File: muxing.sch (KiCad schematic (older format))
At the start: 0 parts

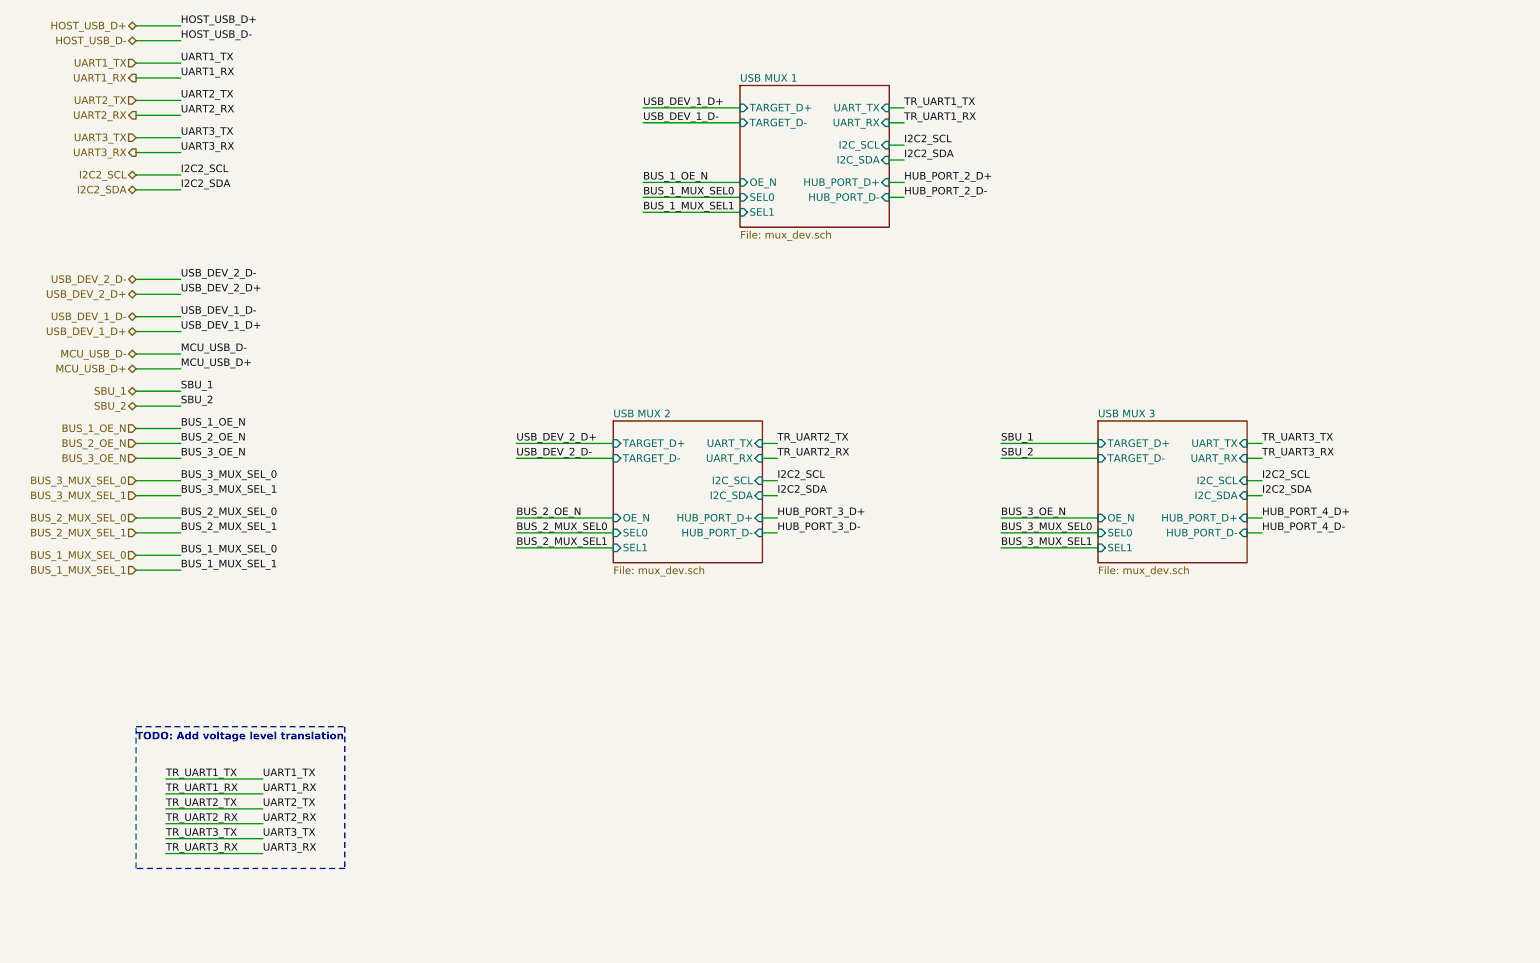
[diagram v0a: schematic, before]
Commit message: Complete muxing and level translation
Added Aux USB to avoid using a HUB, which don't seem to be too readily
available out there and would complicate the design for no good reason.

Now the i2c lines can also be switched.

Added voltage level translation up to 1.2V from 3.3V. Selected
bidirectional level translator.

Started looking into power supply.
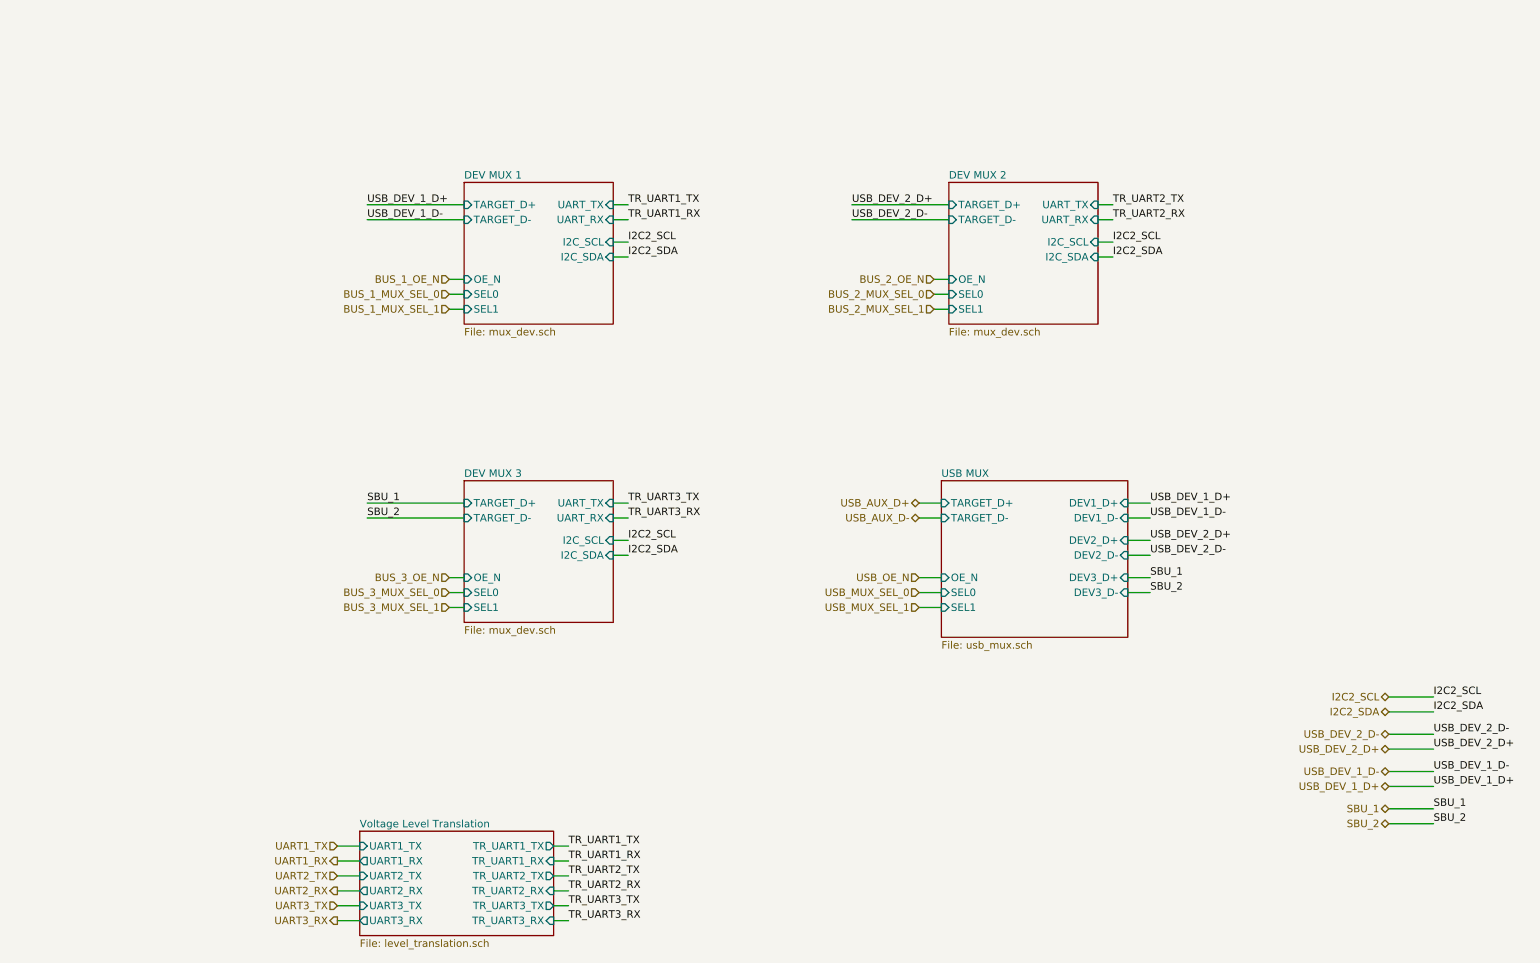
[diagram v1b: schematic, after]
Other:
- note removed: "TODO: Add voltage level translation"

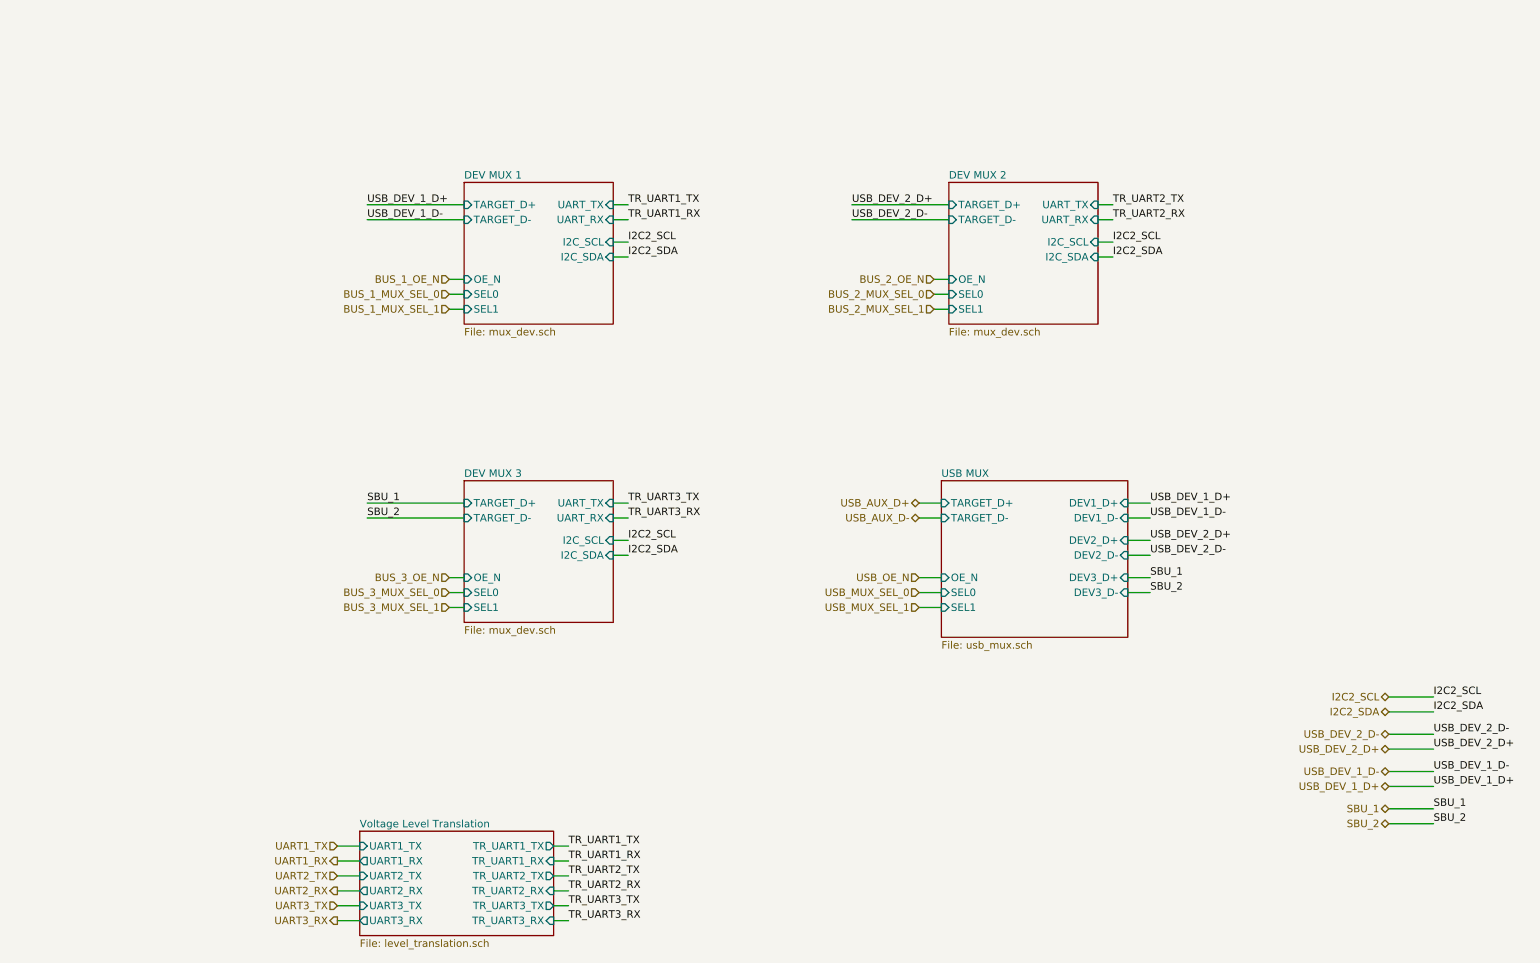
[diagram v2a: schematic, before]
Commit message: Supply caps, initial signal states and headers
  * Added bulk supply caps.
  * Set initial control signal states via resistors.
  * Add debug headers.
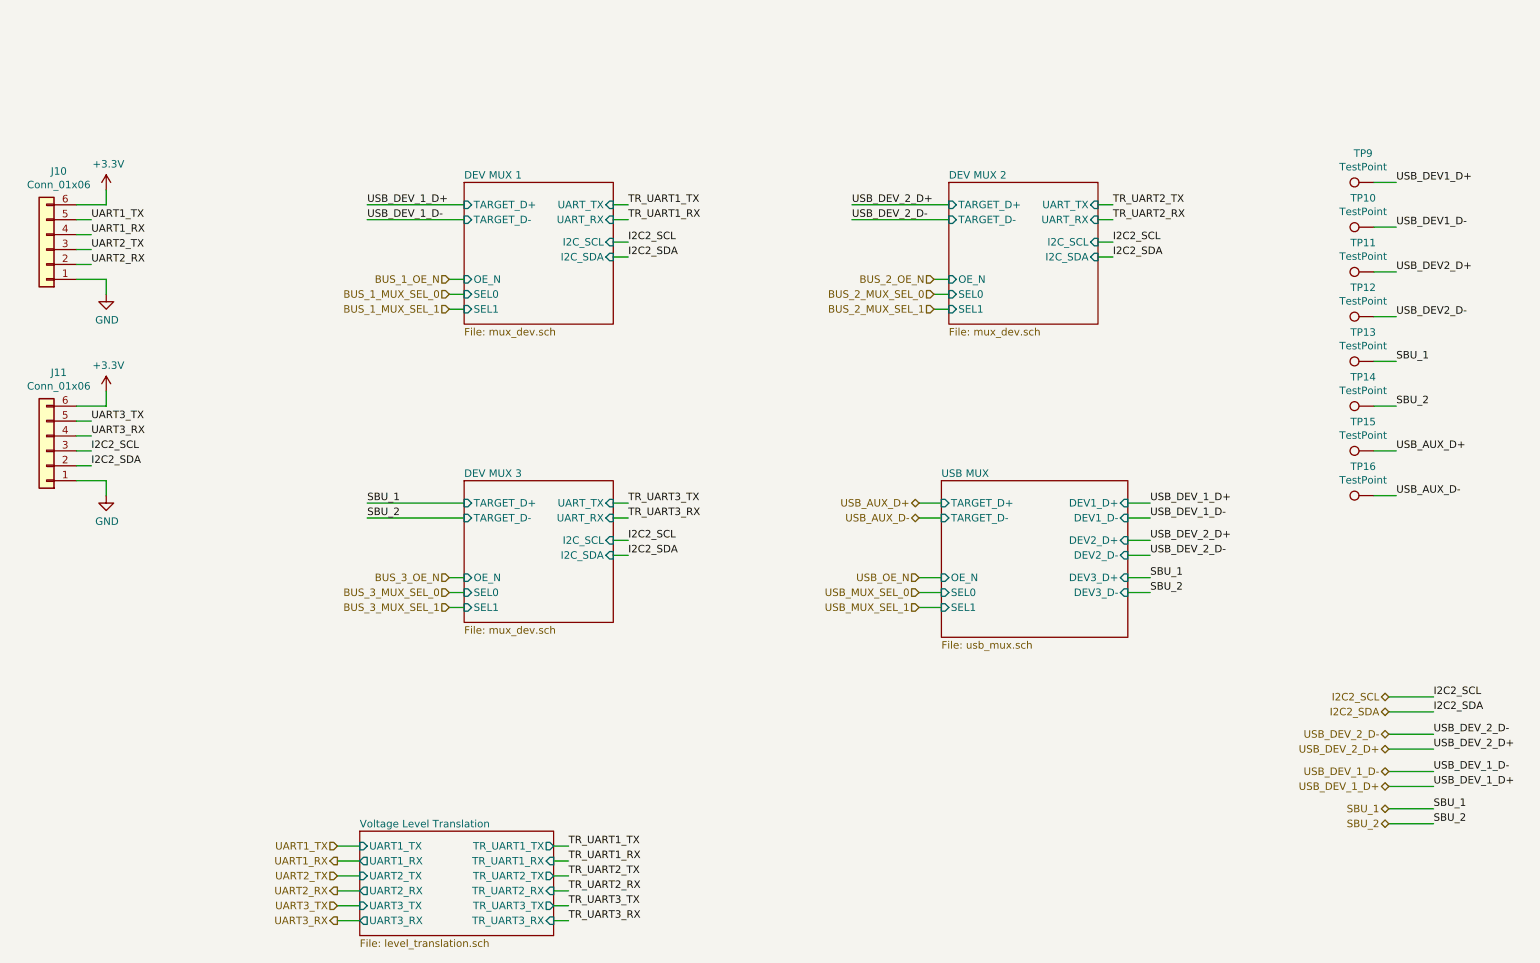
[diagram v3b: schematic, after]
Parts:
- added J10, J11: Conn_01x06, symbol Connector_Generic:Conn_01x06
- added TP10, TP11, TP12, TP13, TP14, TP15, TP16, TP9: TestPoint, symbol Connector:TestPoint
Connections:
- net I2C2_SCL: now also J11.3 (Pin_3)
- net I2C2_SDA: now also J11.2 (Pin_2)
- net SBU_1: now also TP13.1
- net SBU_2: now also TP14.1
- net UART1_RX: now also J10.4 (Pin_4)
- net UART1_TX: now also J10.5 (Pin_5)
- net UART2_RX: now also J10.2 (Pin_2)
- net UART2_TX: now also J10.3 (Pin_3)
- net UART3_RX: now also J11.4 (Pin_4)
- net UART3_TX: now also J11.5 (Pin_5)
- net USB_AUX_D+: now also TP15.1
- net USB_AUX_D-: now also TP16.1
- new net +3V3: J10.6 (Pin_6), J11.6 (Pin_6)
- new net GND: J10.1 (Pin_1), J11.1 (Pin_1)
- new net USB_DEV1_D+: TP9.1
- new net USB_DEV1_D-: TP10.1
- new net USB_DEV2_D+: TP11.1
- new net USB_DEV2_D-: TP12.1
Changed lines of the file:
@@
 Wire Wire Line
 	3750 4850 3850 4850
+Text Label 1350 2250 0    50   ~ 0
+UART1_TX
+Text Label 1350 2350 0    50   ~ 0
+UART1_RX
+Text Label 1350 2450 0    50   ~ 0
+UART2_TX
+Text Label 1350 2550 0    50   ~ 0
+UART2_RX
+Text Label 1350 3600 0    50   ~ 0
+UART3_TX
+Text Label 1350 3700 0    50   ~ 0
+UART3_RX
+$Comp
+L power:+3.3V #PWR019
+U 1 1 61A2A473
+P 1450 2050
+F 0 "#PWR019" H 1450 1900 50  0001 C CNN
+F 1 "+3.3V" H 1465 2223 50  0000 C CNN
+F 2 "" H 1450 2050 50  0001 C CNN
+F 3 "" H 1450 2050 50  0001 C CNN
+	1    1450 2050
+	1    0    0    -1
+$EndComp
+$Comp
+L power:GND #PWR021
+U 1 1 61A2AB85
+P 1450 2750
+F 0 "#PWR021" H 1450 2500 50  0001 C CNN
+F 1 "GND" H 1455 2577 50  0000 C CNN
+F 2 "" H 1450 2750 50  0001 C CNN
+F 3 "" H 1450 2750 50  0001 C CNN
+	1    1450 2750
+	1    0    0    -1
+$EndComp
+Wire Wire Line
+	1350 2250 1250 2250
+Wire Wire Line
+	1250 2350 1350 2350
+Wire Wire Line
+	1350 2450 1250 2450
+Wire Wire Line
+	1250 2550 1350 2550
+Wire Wire Line
+	1350 3600 1250 3600
+Wire Wire Line
+	1250 3700 1350 3700
+Wire Wire Line
+	1250 2650 1450 2650
+Wire Wire Line
+	1450 2650 1450 2750
+Wire Wire Line
+	1450 2050 1450 2150
+Wire Wire Line
+	1450 2150 1250 2150
+$Comp
+L power:+3.3V #PWR023
+U 1 1 61A3EEDE
+P 1450 3400
+F 0 "#PWR023" H 1450 3250 50  0001 C CNN
+F 1 "+3.3V" H 1465 3573 50  0000 C CNN
+F 2 "" H 1450 3400 50  0001 C CNN
+F 3 "" H 1450 3400 50  0001 C CNN
+	1    1450 3400
+	1    0    0    -1
+$EndComp
+$Comp
+L power:GND #PWR025
+U 1 1 61A3EEE4
+P 1450 4100
+F 0 "#PWR025" H 1450 3850 50  0001 C CNN
+F 1 "GND" H 1455 3927 50  0000 C CNN
+F 2 "" H 1450 4100 50  0001 C CNN
+F 3 "" H 1450 4100 50  0001 C CNN
+	1    1450 4100
+	1    0    0    -1
+$EndComp
+Wire Wire Line
+	1250 4000 1450 4000
+Wire Wire Line
+	1450 4000 1450 4100
+Wire Wire Line
+	1450 3400 1450 3500
+Wire Wire Line
+	1450 3500 1250 3500
+$Comp
+L Connector_Generic:Conn_01x06 J11
+U 1 1 61A4FE69
+P 1050 3800
+F 0 "J11" H 968 3275 50  0000 C CNN
+F 1 "Conn_01x06" H 968 3366 50  0000 C CNN
+F 2 "" H 1050 3800 50  0001 C CNN
+F 3 "~" H 1050 3800 50  0001 C CNN
+	1    1050 3800
+	-1   0    0    1
+$EndComp
+$Comp
+L Connector_Generic:Conn_01x06 J10
+U 1 1 61A546CA
+P 1050 2450
+F 0 "J10" H 968 1925 50  0000 C CNN
+F 1 "Conn_01x06" H 968 2016 50  0000 C CNN
+F 2 "" H 1050 2450 50  0001 C CNN
+F 3 "~" H 1050 2450 50  0001 C CNN
+	1    1050 2450
+	-1   0    0    1
+$EndComp
+Text Label 1350 3800 0    50   ~ 0
+I2C2_SCL
+Text Label 1350 3900 0    50   ~ 0
+I2C2_SDA
+Wire Wire Line
+	1350 3800 1250 3800
+Wire Wire Line
+	1250 3900 1350 3900
+$Comp
+L Connector:TestPoint TP9
+U 1 1 61A8EFBE
+P 9950 2000
+F 0 "TP9" V 10145 2072 50  0000 C CNN
+F 1 "TestPoint" V 10054 2072 50  0000 C CNN
+F 2 "" H 10150 2000 50  0001 C CNN
+F 3 "~" H 10150 2000 50  0001 C CNN
+	1    9950 2000
+	0    -1   -1   0
+$EndComp
+Text Label 10100 2000 0    50   ~ 0
+USB_DEV1_D+
+$Comp
+L Connector:TestPoint TP10
+U 1 1 61A90758
+P 9950 2300
+F 0 "TP10" V 10145 2372 50  0000 C CNN
+F 1 "TestPoint" V 10054 2372 50  0000 C CNN
+F 2 "" H 10150 2300 50  0001 C CNN
+F 3 "~" H 10150 2300 50  0001 C CNN
+	1    9950 2300
+	0    -1   -1   0
+$EndComp
+Text Label 10100 2300 0    50   ~ 0
+USB_DEV1_D-
+$Comp
+L Connector:TestPoint TP11
+U 1 1 61A93BF3
+P 9950 2600
+F 0 "TP11" V 10145 2672 50  0000 C CNN
+F 1 "TestPoint" V 10054 2672 50  0000 C CNN
+F 2 "" H 10150 2600 50  0001 C CNN
+F 3 "~" H 10150 2600 50  0001 C CNN
+	1    9950 2600
+	0    -1   -1   0
+$EndComp
+Text Label 10100 2600 0    50   ~ 0
+USB_DEV2_D+
+$Comp
+L Connector:TestPoint TP12
+U 1 1 61A96FF2
+P 9950 2900
+F 0 "TP12" V 10145 2972 50  0000 C CNN
+F 1 "TestPoint" V 10054 2972 50  0000 C CNN
+F 2 "" H 10150 2900 50  0001 C CNN
+F 3 "~" H 10150 2900 50  0001 C CNN
+	1    9950 2900
+	0    -1   -1   0
+$EndComp
+Text Label 10100 2900 0    50   ~ 0
+USB_DEV2_D-
+$Comp
+L Connector:TestPoint TP13
+U 1 1 61A9A32F
+P 9950 3200
+F 0 "TP13" V 10145 3272 50  0000 C CNN
+F 1 "TestPoint" V 10054 3272 50  0000 C CNN
+F 2 "" H 10150 3200 50  0001 C CNN
+F 3 "~" H 10150 3200 50  0001 C CNN
+	1    9950 3200
+	0    -1   -1   0
+$EndComp
+Text Label 10100 3200 0    50   ~ 0
+SBU_1
+$Comp
+L Connector:TestPoint TP14
+U 1 1 61A9D6B6
+P 9950 3500
+F 0 "TP14" V 10145 3572 50  0000 C CNN
+F 1 "TestPoint" V 10054 3572 50  0000 C CNN
+F 2 "" H 10150 3500 50  0001 C CNN
+F 3 "~" H 10150 3500 50  0001 C CNN
+	1    9950 3500
+	0    -1   -1   0
+$EndComp
+Text Label 10100 3500 0    50   ~ 0
+SBU_2
+Wire Wire Line
+	9950 2000 10100 2000
+Wire Wire Line
+	10100 2300 9950 2300
+Wire Wire Line
+	10100 2600 9950 2600
+Wire Wire Line
+	9950 2900 10100 2900
+Wire Wire Line
+	10100 3200 9950 3200
+Wire Wire Line
+	9950 3500 10100 3500
+$Comp
+L Connector:TestPoint TP15
+U 1 1 61AC146D
+P 9950 3800
+F 0 "TP15" V 10145 3872 50  0000 C CNN
+F 1 "TestPoint" V 10054 3872 50  0000 C CNN
+F 2 "" H 10150 3800 50  0001 C CNN
+F 3 "~" H 10150 3800 50  0001 C CNN
+	1    9950 3800
+	0    -1   -1   0
+$EndComp
+Text Label 10100 3800 0    50   ~ 0
+USB_AUX_D+
+$Comp
+L Connector:TestPoint TP16
+U 1 1 61AC1474
+P 9950 4100
+F 0 "TP16" V 10145 4172 50  0000 C CNN
+F 1 "TestPoint" V 10054 4172 50  0000 C CNN
+F 2 "" H 10150 4100 50  0001 C CNN
+F 3 "~" H 10150 4100 50  0001 C CNN
+	1    9950 4100
+	0    -1   -1   0
+$EndComp
+Text Label 10100 4100 0    50   ~ 0
+USB_AUX_D-
+Wire Wire Line
+	10100 3800 9950 3800
+Wire Wire Line
+	9950 4100 10100 4100
 $EndSCHEMATC
